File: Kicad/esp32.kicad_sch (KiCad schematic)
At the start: 8 parts, among them J11 PROG, SW1 RESET, SW4 BOOT, U4 ESP32-WROOM-32D

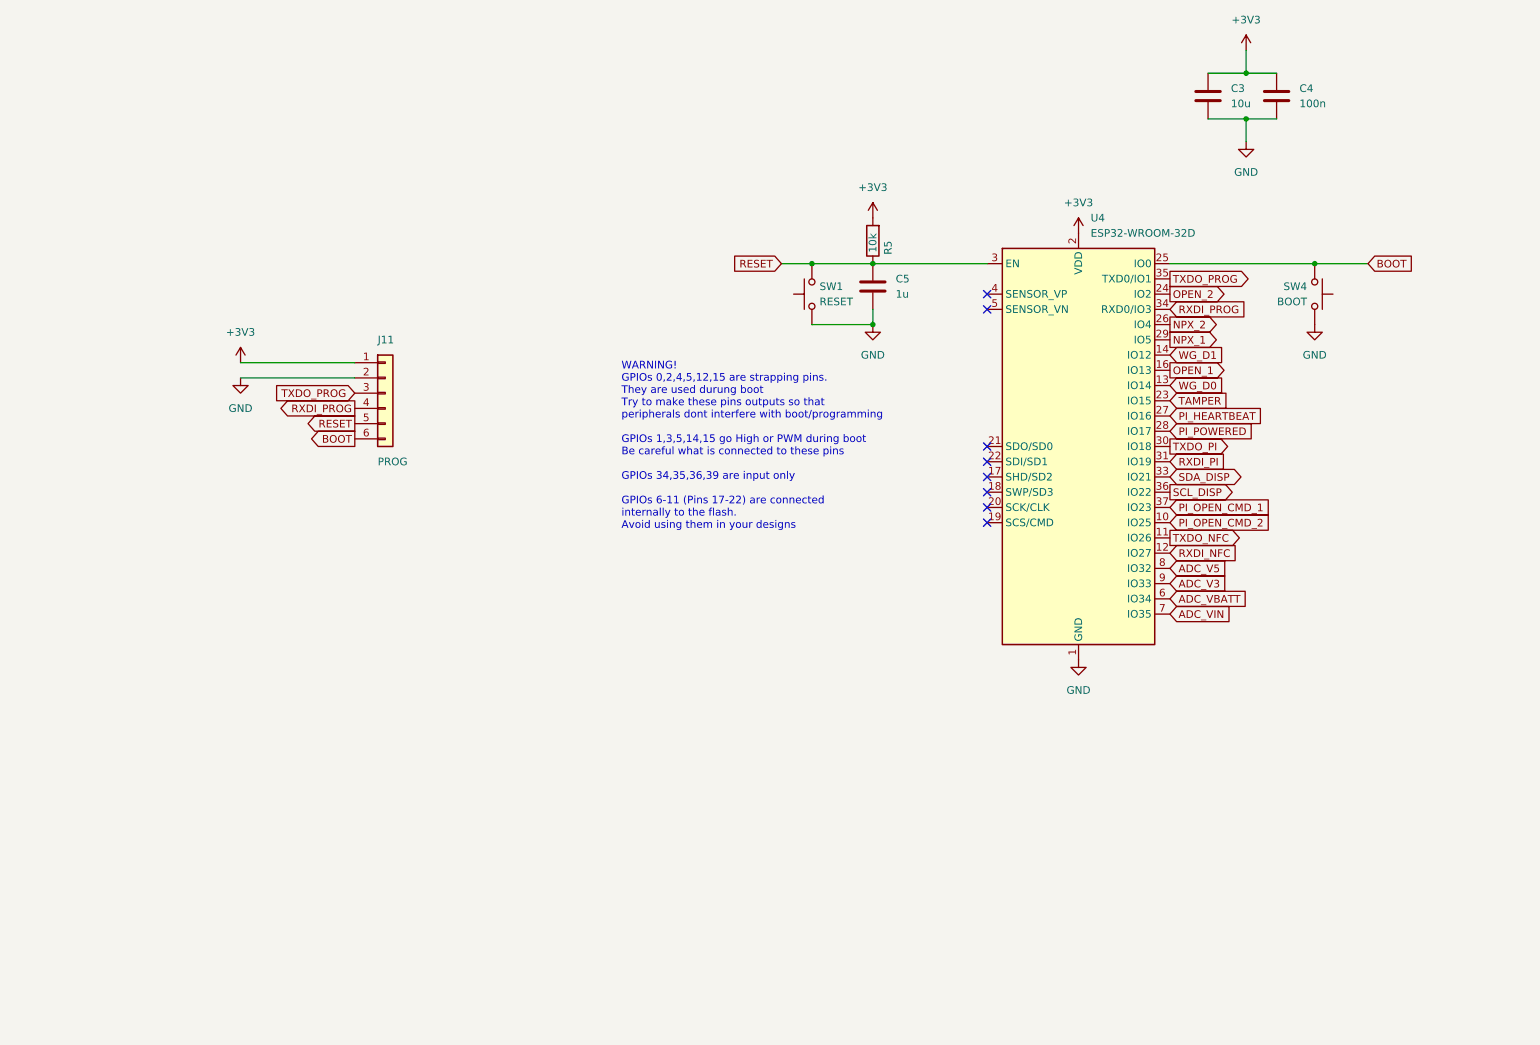
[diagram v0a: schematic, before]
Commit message: Rework of power circuits to improve protection
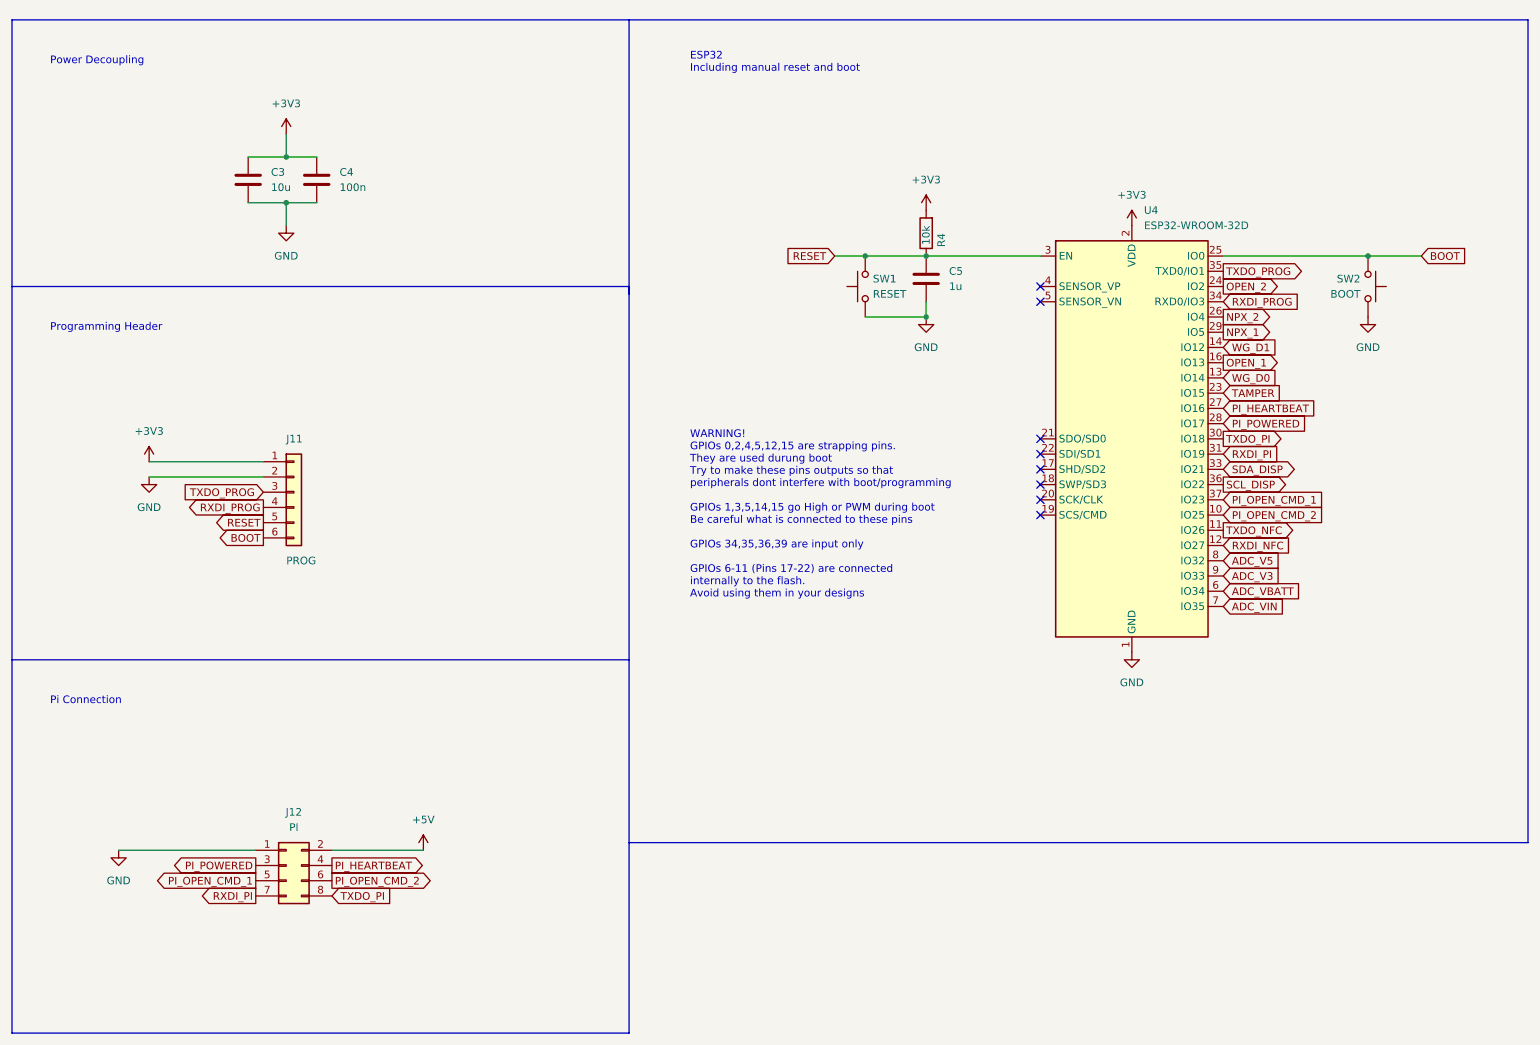
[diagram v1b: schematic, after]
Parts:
- added J12: PI, Connector_IDC:IDC-Header_2x04_P2.54mm_Vertical, symbol Connector_Generic:Conn_02x04_Odd_Even
- renumbered R5 to R4, SW4 to SW2
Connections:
- net GND: now also J12.1 (Pin_1)
- net PI_HEARTBEAT: now also J12.4 (Pin_4)
- net PI_OPEN_CMD_1: now also J12.5 (Pin_5)
- net PI_OPEN_CMD_2: now also J12.6 (Pin_6)
- net PI_POWERED: now also J12.3 (Pin_3)
- net RXDI_PI: now also J12.7 (Pin_7)
- net TXDO_PI: now also J12.8 (Pin_8)
- new net +5V: J12.2 (Pin_2)
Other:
- note added: "ESP32 Including manual reset and boot"
- note added: "Pi Connection"
- note added: "Power Decoupling"
- note added: "Programming Header"
- moved on the sheet: C3, C4, C5, J11, R4, SW1, SW2, U4
